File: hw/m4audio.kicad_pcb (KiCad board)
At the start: 2 copper layers, 46 x 46 mm, 74 parts, among them J1 JACK_TRS, J11 CONN_01X03, J2 JACK_TRS, J21 CONN_01X03, P1 CONN_01X02, P2 USB_OTG, P3 CONN_02X05, P4 CONN_01X08, P5 CONN_01X03, U1 LD1117S33TR, U2 STM32F405RG, U3 AD8542, U4 WM8731, Y1 Crystal

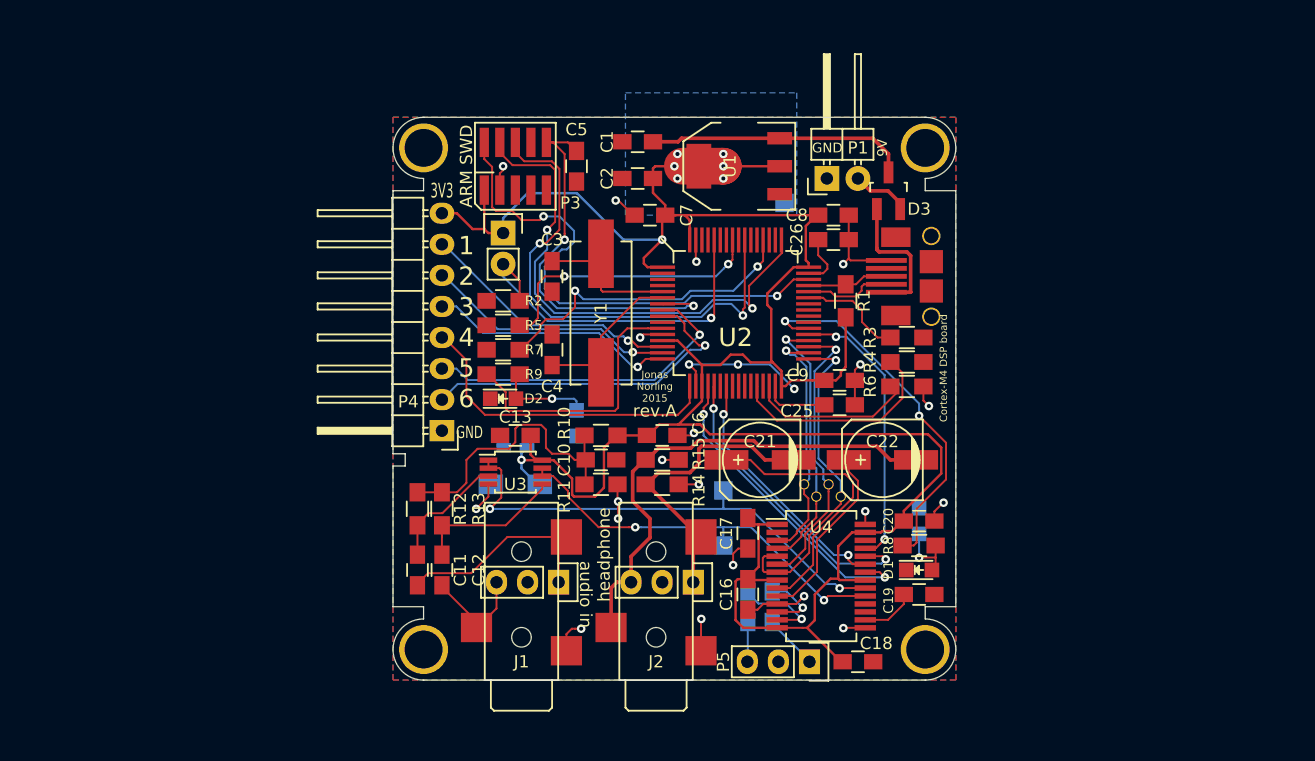
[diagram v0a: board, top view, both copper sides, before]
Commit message: Board update and ripup: split power supply, 49.5mm size
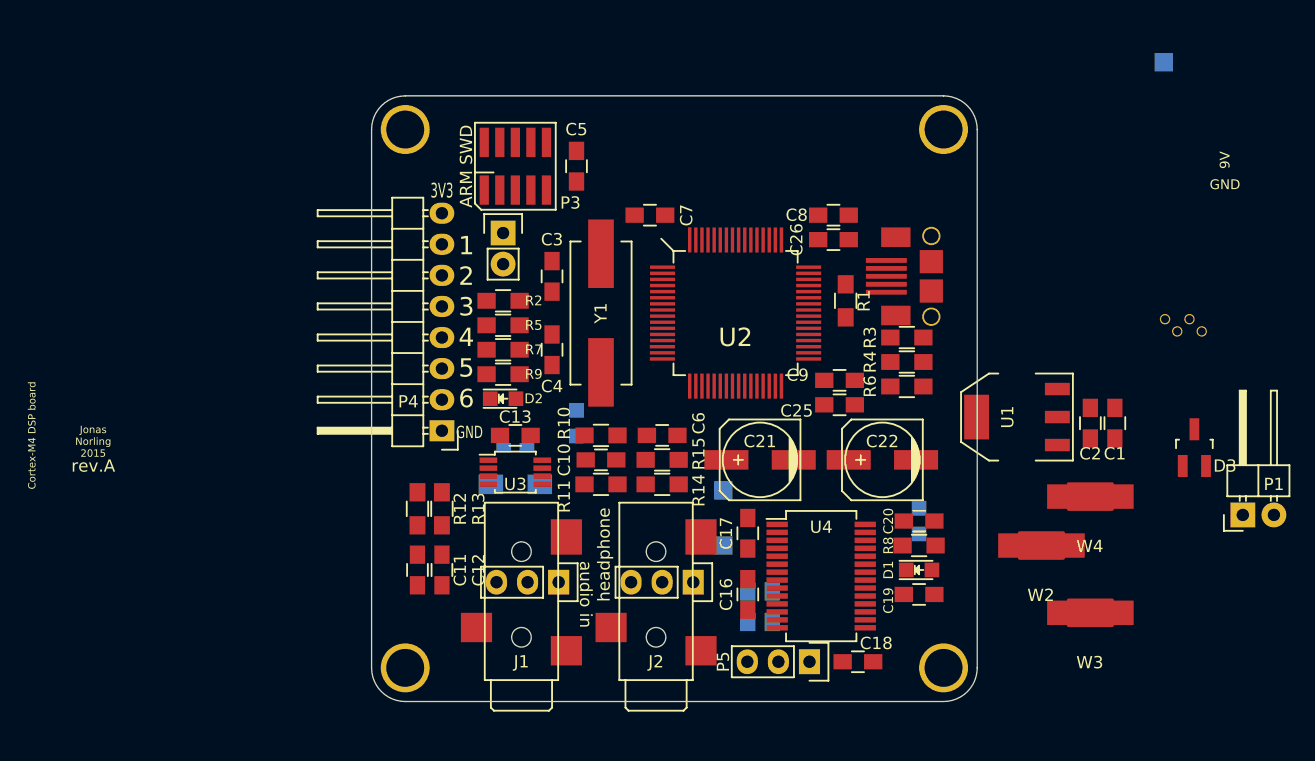
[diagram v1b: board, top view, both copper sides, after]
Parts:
- added W2: V_A, Oddities:NetTie-I_Connected_SMD, F.Cu at (166.0, 127.0)
- added W3: V_D, Oddities:NetTie-I_Connected_SMD, F.Cu at (170.0, 132.5)
- added W4: V_HP, Oddities:NetTie-I_Connected_SMD, F.Cu at (170.0, 123.0)
- R12, R13: value 500k -> 560k
- moved C1 45.3 mm to (172.0, 117.0), turned to 270 degrees
- moved REF** 45.2 mm to (90.0, 111.0)
- moved P1 43.7 mm to (182.5, 124.5)
- moved C2 42.1 mm to (170.0, 117.0), turned to 270 degrees
- moved OSHW 41.2 mm to (90.5, 98.0)
- moved TP1 33.1 mm to (176.0, 87.5)
- moved D3 32.6 mm to (178.5, 119.0)
- moved TP5 32.4 mm to (177.1, 109.5)
- moved TP6 32.4 mm to (179.1, 109.5)
- moved TP7 32.4 mm to (178.1, 108.5)
- moved TP8 32.4 mm to (176.1, 108.5)
- moved U1 30.6 mm to (164.0, 116.5)
- moved REF** 2.12 mm to (114.0, 93.0)
- moved REF** 2.12 mm to (158.0, 93.0)
- moved REF** 2.12 mm to (114.0, 137.0)
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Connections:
- C13 pad 2: VDD -> VAA
- C14 pad 2: VDD -> VAA
- C15 pad 2: VDD -> VAA
- C16 pad 2: VDD -> HPVDD
- C17 pad 2: VDD -> VAA
- C18 pad 2: VDD -> VAA
- C2 pad 1: VDD -> Net-(C2-Pad1)
- C20 pad 2: VDD -> VAA
- P2 pad 4: /USB_ID -> (no net)
- P3 pad 7: Net-(P3-Pad7) -> (no net)
- P3 pad 8: Net-(P3-Pad8) -> (no net)
- R10 pad 2: VDD -> VAA
- TP1 pad 1: VDD -> Net-(C2-Pad1)
- U1 pad 2: VDD -> Net-(C2-Pad1)
- U2 pad 10: Net-(U2-Pad10) -> (no net)
- U2 pad 2: Net-(U2-Pad2) -> (no net)
- U2 pad 22: Net-(U2-Pad22) -> (no net)
- U2 pad 24: Net-(U2-Pad24) -> (no net)
- U2 pad 25: Net-(U2-Pad25) -> (no net)
- U2 pad 26: Net-(U2-Pad26) -> (no net)
- U2 pad 27: Net-(U2-Pad27) -> (no net)
- U2 pad 29: Net-(U2-Pad29) -> (no net)
- U2 pad 3: Net-(U2-Pad3) -> (no net)
- U2 pad 39: Net-(U2-Pad39) -> (no net)
- U2 pad 4: Net-(U2-Pad4) -> (no net)
- U2 pad 40: Net-(U2-Pad40) -> (no net)
- U2 pad 41: Net-(U2-Pad41) -> (no net)
- U2 pad 42: Net-(U2-Pad42) -> (no net)
- U2 pad 50: Net-(U2-Pad50) -> (no net)
- U2 pad 51: Net-(U2-Pad51) -> (no net)
- U2 pad 53: Net-(U2-Pad53) -> (no net)
- U2 pad 54: Net-(U2-Pad54) -> (no net)
- U2 pad 56: Net-(U2-Pad56) -> (no net)
- U2 pad 58: Net-(U2-Pad58) -> (no net)
- U2 pad 59: Net-(U2-Pad59) -> (no net)
- U2 pad 61: Net-(U2-Pad61) -> (no net)
- U2 pad 62: Net-(U2-Pad62) -> (no net)
- U3 pad 8: VDD -> VAA
- U4 pad 1: VDD -> VAA
- U4 pad 14: VDD -> VAA
- U4 pad 17: Net-(U4-Pad17) -> (no net)
- U4 pad 18: Net-(U4-Pad18) -> (no net)
- U4 pad 2: Net-(U4-Pad2) -> (no net)
- U4 pad 21: VDD -> VAA
- U4 pad 26: Net-(U4-Pad26) -> (no net)
- U4 pad 27: VDD -> VAA
- U4 pad 8: VDD -> HPVDD
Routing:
- net VDD: track 209.1 -> 0.00 mm, vias 8 -> 0
- net GND: track 59.0 -> 0.00 mm, vias 23 -> 0
- net /SWCLK: track 42.7 -> 0.00 mm, vias 2 -> 0
- net /SWDIO: track 42.1 -> 0.00 mm, vias 2 -> 0
- net /SWO: track 41.8 -> 0.00 mm, vias 2 -> 0
- net /audio/AOUT_R: track 40.3 -> 0.00 mm
- net /audio/ADCL: track 40.2 -> 0.00 mm, vias 2 -> 0
- net /audio/ADCR: track 33.2 -> 0.00 mm, vias 2 -> 0
- net /NRST: track 32.6 -> 0.00 mm, vias 2 -> 0
- net /LED1: track 30.7 -> 0.00 mm, vias 2 -> 0
- net /BOOT0: track 29.7 -> 0.00 mm, vias 1 -> 0
- net /MISC6: track 28.2 -> 0.00 mm, vias 1 -> 0
- net /audio/ADCLR: track 27.2 -> 0.00 mm, vias 1 -> 0
- net /MISC5: track 27.0 -> 0.00 mm, vias 1 -> 0
- net /MISC4: track 26.4 -> 0.00 mm
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- removed copper zone on B.Cu, net GND
- removed copper zone on F.Cu, net GND
- removed copper zone on B.Cu, net VDD
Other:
- board size 46 x 46 mm -> 49.5 x 49.5 mm

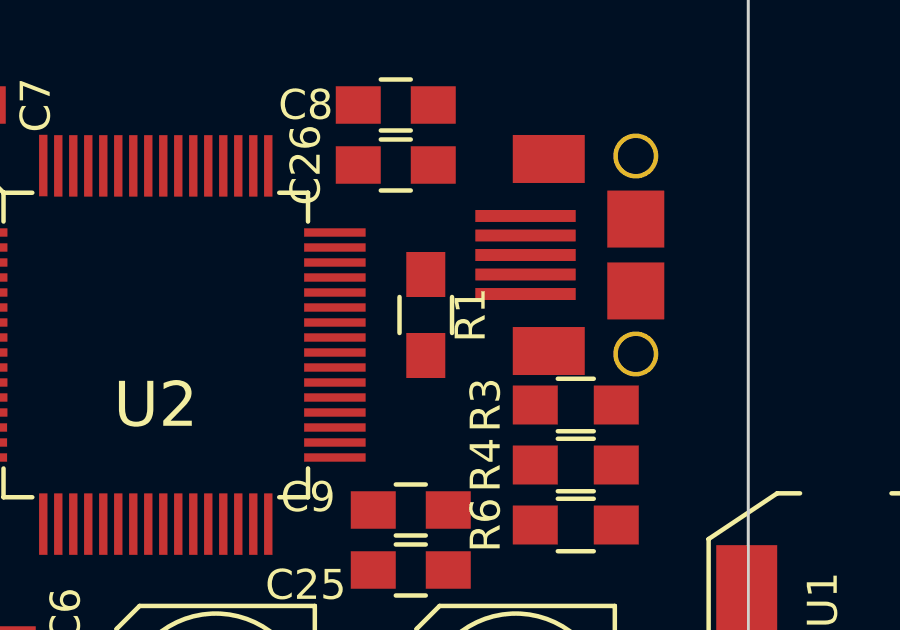
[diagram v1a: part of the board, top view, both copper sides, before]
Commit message: Remove USB resistor, the STM32 has one built in
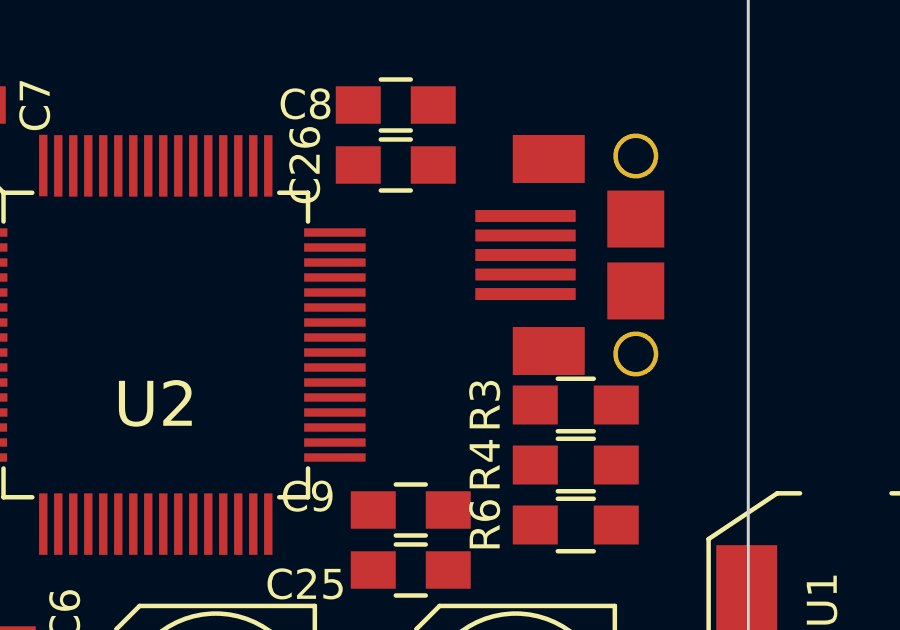
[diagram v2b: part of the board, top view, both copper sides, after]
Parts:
- removed R1: DNP, Resistors_SMD:R_0805_HandSoldering
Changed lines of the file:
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@@
-(kicad_pcb (version 4) (host pcbnew 0.201509231831+6209~30~ubuntu14.04.1-product)
+(kicad_pcb (version 4) (host pcbnew 0.201509251832+6217~30~ubuntu14.04.1-product)
   (general
-    (links 166)
+    (links 164)
     (no_connects 164)
-    (area 112.949999 91.949999 159.050001 138.050001)
+    (area 111.199999 90.199999 160.800001 139.800001)
     (thickness 1.6)
     (drawings 59)
     (tracks 0)
     (zones 0)
-    (modules 77)
+    (modules 76)
     (nets 59)
   )
@@
     (pad_to_mask_clearance 0)
     (aux_axis_origin 0 0)
-    (visible_elements FFFF2F7F)
+    (visible_elements FFFFEF7F)
     (pcbplotparams
       (layerselection 0x010f0_80000001)
@@
       (rotate (xyz 0 0 0))
     )
-  )
-  (module Resistors_SMD:R_0805_HandSoldering (layer F.Cu)
-    (at 150 107 270)
-    (descr "Resistor SMD 0805, hand soldering")
-    (tags "resistor 0805")
-    (attr smd)
-    (fp_text reference R1 (at 0 -1.5 450) (layer F.SilkS)
-      (effects (font (size 1 1) (thickness 0.15)))
-    )
-    (fp_text value DNP (at 0 2.1 270) (layer F.Fab)
-      (effects (font (size 1 1) (thickness 0.15)))
-    )
-    (fp_line (start -2.4 -1) (end 2.4 -1) (layer F.CrtYd) (width 0.05))
-    (fp_line (start -2.4 1) (end 2.4 1) (layer F.CrtYd) (width 0.05))
-    (fp_line (start -2.4 -1) (end -2.4 1) (layer F.CrtYd) (width 0.05))
-    (fp_line (start 2.4 -1) (end 2.4 1) (layer F.CrtYd) (width 0.05))
-    (fp_line (start 0.6 0.875) (end -0.6 0.875) (layer F.SilkS) (width 0.15))
-    (fp_line (start -0.6 -0.875) (end 0.6 -0.875) (layer F.SilkS) (width 0.15))
-    (pad 1 smd rect (at -1.35 0 270) (size 1.5 1.3) (layers F.Cu F.Paste F.Mask)
-      (net 2 /USB_DP))
-    (pad 2 smd rect (at 1.35 0 270) (size 1.5 1.3) (layers F.Cu F.Paste F.Mask)
-      (net 51 VDD))
-    (model Resistors_SMD.3dshapes/R_0805_HandSoldering.wrl
-      (at (xyz 0 0 0))
-      (scale (xyz 1 1 1))
-      (rotate (xyz 0 0 0))
-    )
